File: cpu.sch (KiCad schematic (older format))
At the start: 11 parts, among them J1 Conn_02x05_Odd_Even, SW2 SW_Push, SW3 SW_Push, U1 E73-2G4M04S-52832

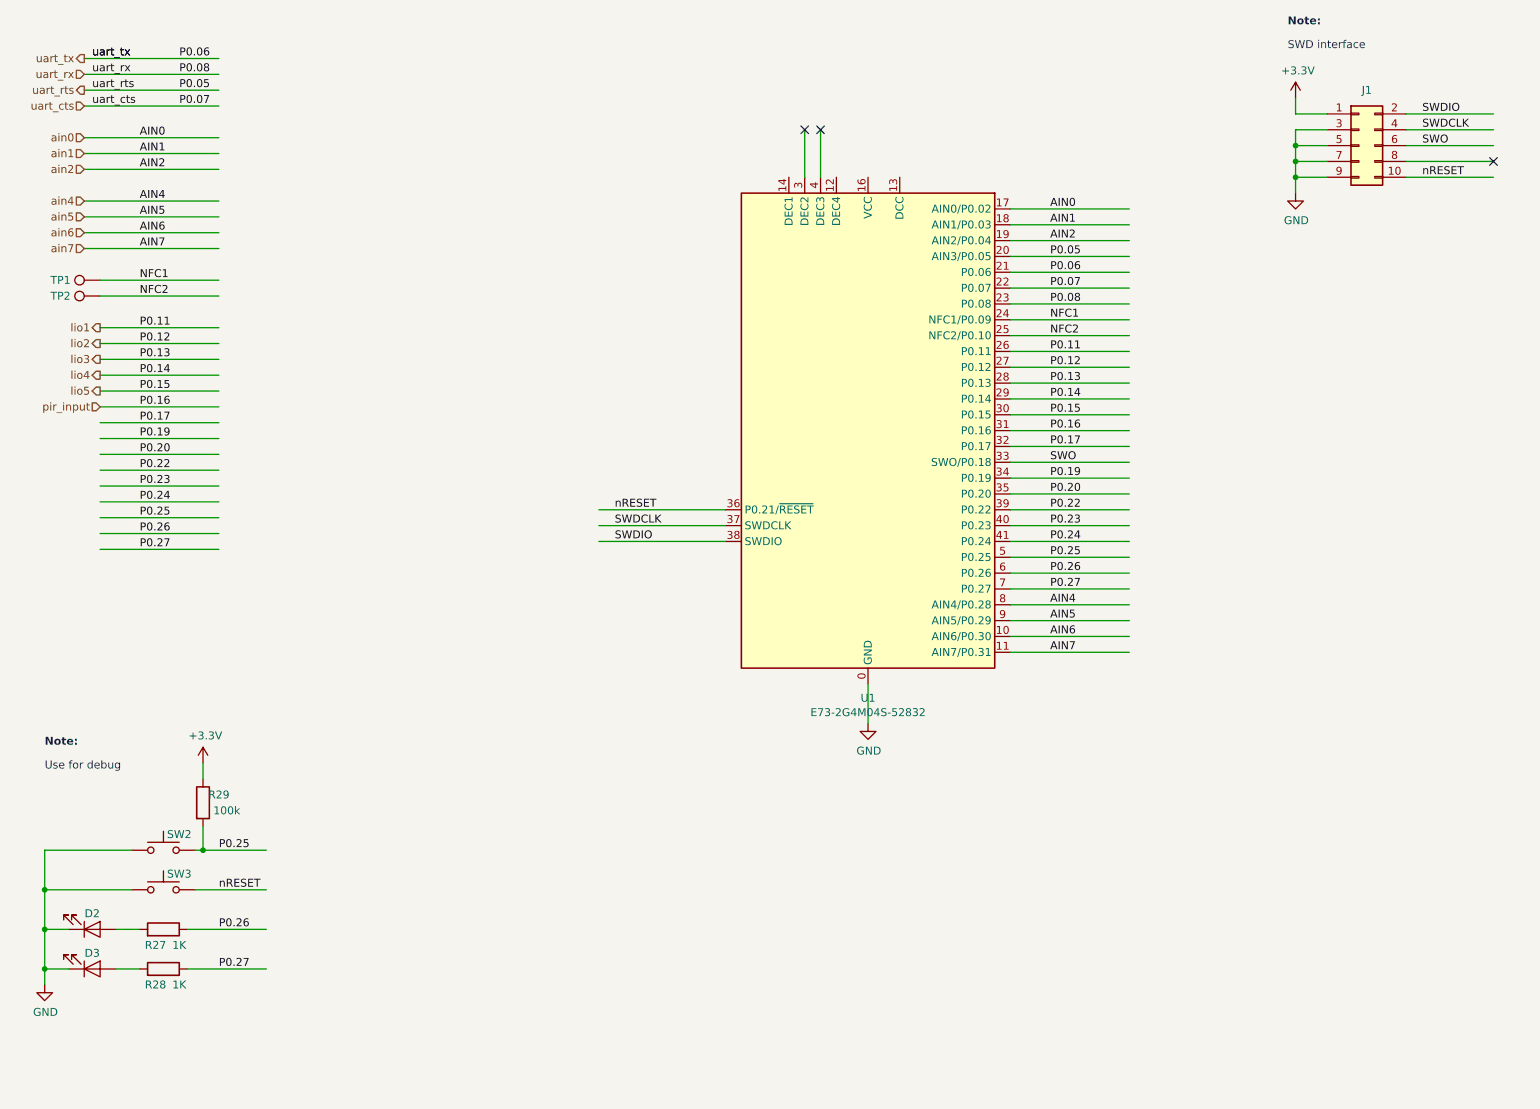
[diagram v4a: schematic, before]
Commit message: more layout + resized pcb to 100 x 80
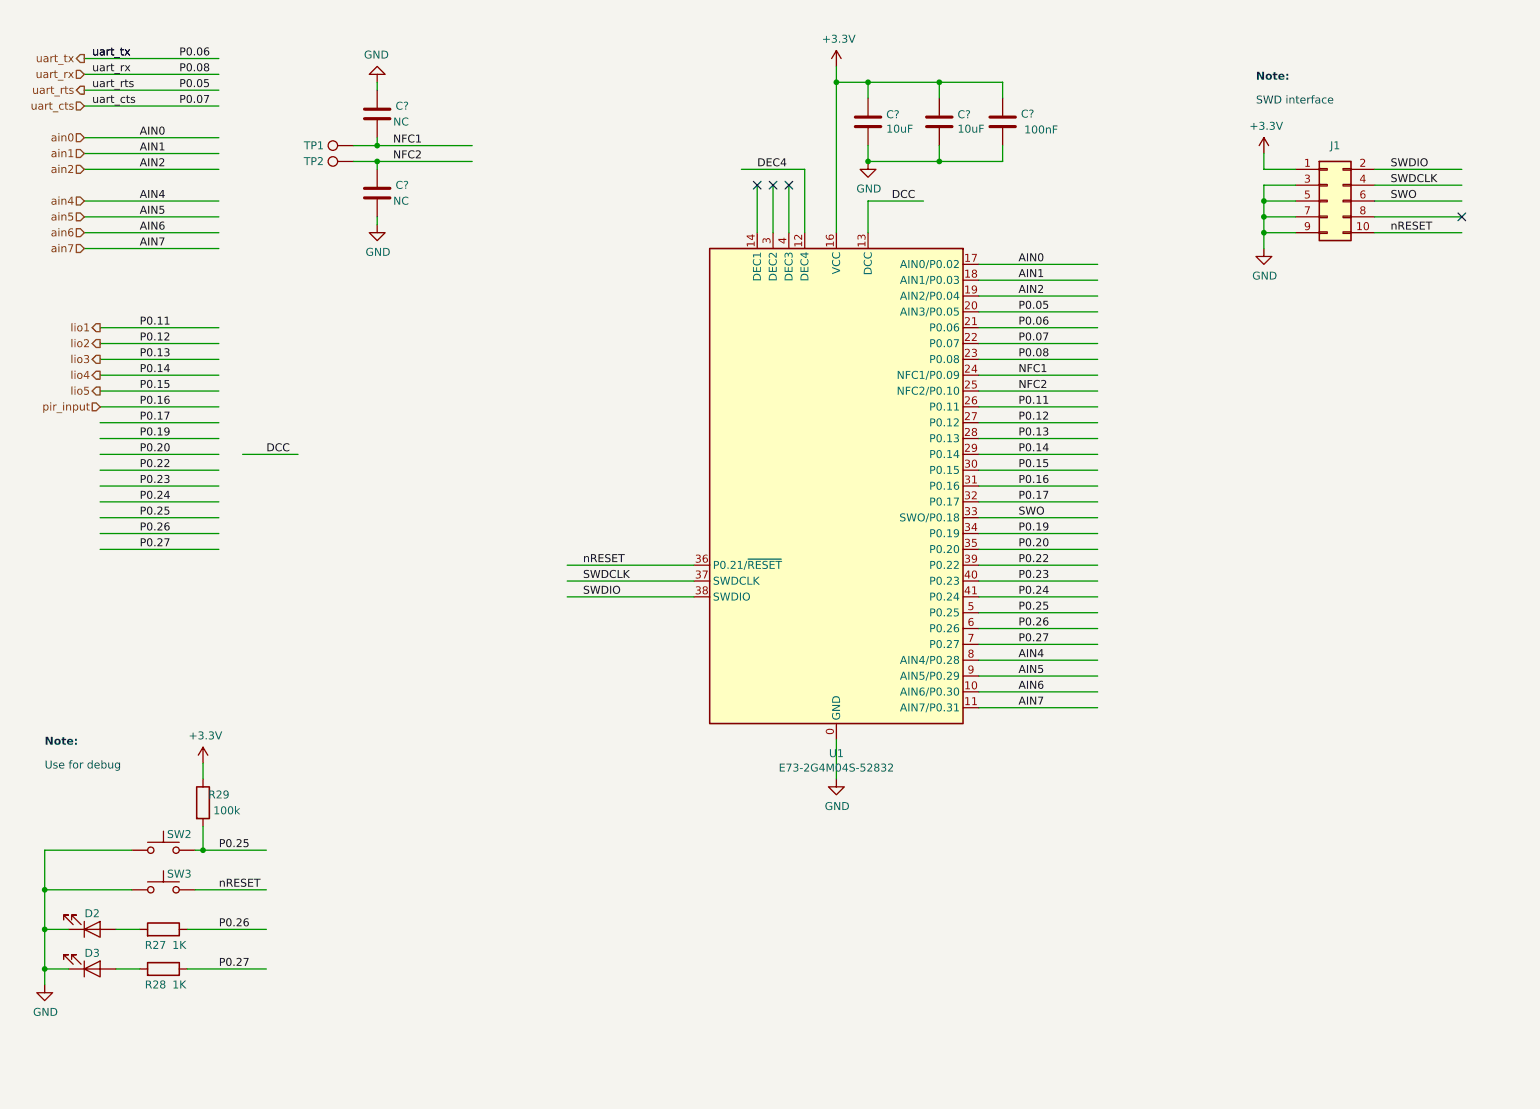
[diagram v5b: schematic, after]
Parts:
- added C? (x2): 10uF, Capacitor_SMD:C_1210_3225Metric_Pad1.42x2.65mm_HandSolder, symbol Device:C
- added C?: 100nF, Capacitor_SMD:C_0805_2012Metric_Pad1.15x1.40mm_HandSolder, symbol Device:C
- added C? (x2): NC, Capacitor_SMD:C_0603_1608Metric, symbol Device:C
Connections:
- net labels added: DCC, DEC4
- wire segments 95 -> 120
- no-connect marks 3 -> 4
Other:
- moved on the sheet: J1, TP1, TP2, U1

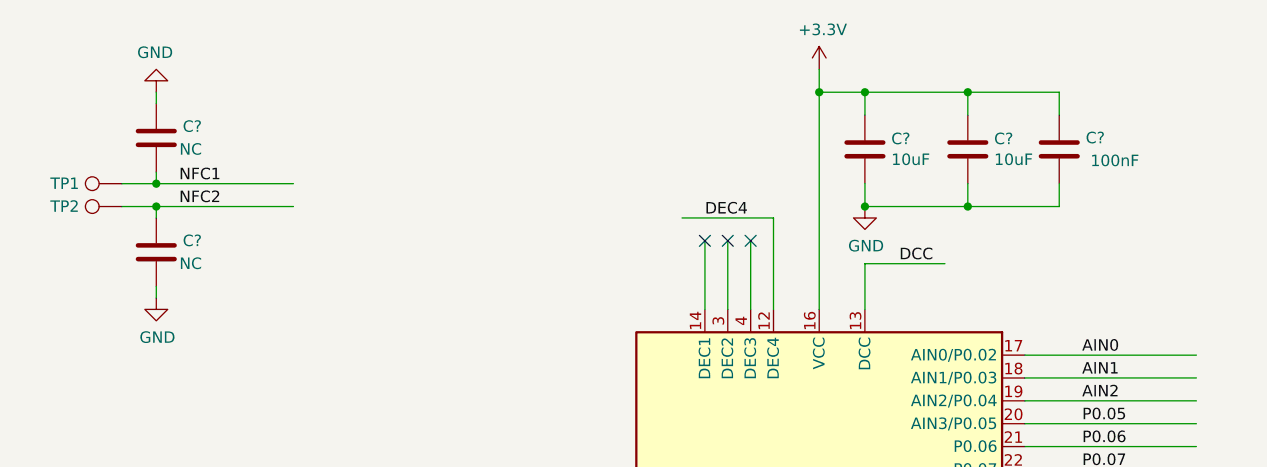
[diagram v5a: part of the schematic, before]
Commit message: changed pcb size to 100 x 70 and made progress on layout
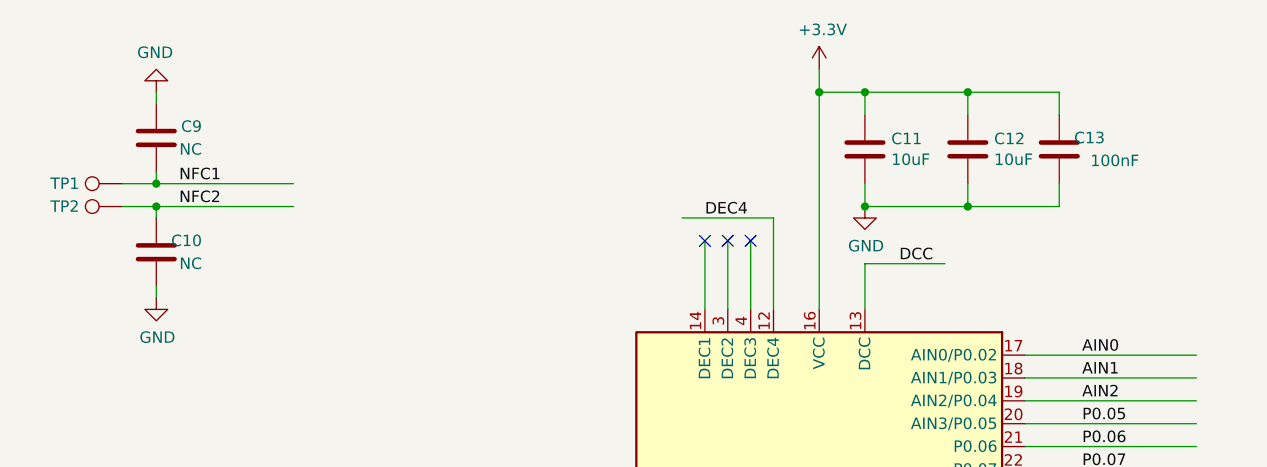
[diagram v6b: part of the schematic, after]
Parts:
- gave numbers to parts that had none: 5
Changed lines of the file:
@@
 P 6600 1500
 AR Path="/5E5BC499/5E9686F9" Ref="C?"  Part="1"
-AR Path="/5E59E010/5E9686F9" Ref="C?"  Part="1"
-F 0 "C?" H 6715 1546 50  0000 L CNN
+AR Path="/5E59E010/5E9686F9" Ref="C11"  Part="1"
+F 0 "C11" H 6715 1546 50  0000 L CNN
 F 1 "10uF" H 6715 1455 50  0000 L CNN
 F 2 "Capacitor_SMD:C_1210_3225Metric_Pad1.42x2.65mm_HandSolder" H 6638 1350 50  0001 C CNN
@@
 P 7050 1500
 AR Path="/5E5BC499/5E96C802" Ref="C?"  Part="1"
-AR Path="/5E59E010/5E96C802" Ref="C?"  Part="1"
-F 0 "C?" H 7165 1546 50  0000 L CNN
+AR Path="/5E59E010/5E96C802" Ref="C12"  Part="1"
+F 0 "C12" H 7165 1546 50  0000 L CNN
 F 1 "10uF" H 7165 1455 50  0000 L CNN
 F 2 "Capacitor_SMD:C_1210_3225Metric_Pad1.42x2.65mm_HandSolder" H 7088 1350 50  0001 C CNN
@@
 P 6400 1150
 AR Path="/5E97CE9F" Ref="#PWR?"  Part="1"
-AR Path="/5E59E010/5E97CE9F" Ref="#PWR?"  Part="1"
-F 0 "#PWR?" H 6400 1000 50  0001 C CNN
+AR Path="/5E59E010/5E97CE9F" Ref="#PWR0134"  Part="1"
+F 0 "#PWR0134" H 6400 1000 50  0001 C CNN
 F 1 "+3.3V" H 6415 1323 50  0000 C CNN
 F 2 "" H 6400 1150 50  0001 C CNN
@@
 AR Path="/5E5BC499/5E983FD2" Ref="C?"  Part="1"
 AR Path="/5E8399F7/5E983FD2" Ref="C?"  Part="1"
-AR Path="/5E59E010/5E983FD2" Ref="C?"  Part="1"
-F 0 "C?" H 7250 1450 50  0000 L CNN
+AR Path="/5E59E010/5E983FD2" Ref="C13"  Part="1"
+F 0 "C13" H 7250 1450 50  0000 L CNN
 F 1 "100nF" H 7100 1550 50  0000 L CNN
 F 2 "Capacitor_SMD:C_0805_2012Metric_Pad1.15x1.40mm_HandSolder" H 7488 1350 50  0001 C CNN
@@
 AR Path="/5E5BC499/5E9917BA" Ref="C?"  Part="1"
 AR Path="/5E8399F7/5E9917BA" Ref="C?"  Part="1"
-AR Path="/5E59E010/5E9917BA" Ref="C?"  Part="1"
-F 0 "C?" H 3300 1900 50  0000 L CNN
+AR Path="/5E59E010/5E9917BA" Ref="C10"  Part="1"
+F 0 "C10" H 3300 1900 50  0000 L CNN
 F 1 "NC" H 3300 2000 50  0000 L CNN
 F 2 "Capacitor_SMD:C_0603_1608Metric" H 3538 1800 50  0001 C CNN
@@
 AR Path="/5E5BC499/5E995EA1" Ref="C?"  Part="1"
 AR Path="/5E8399F7/5E995EA1" Ref="C?"  Part="1"
-AR Path="/5E59E010/5E995EA1" Ref="C?"  Part="1"
-F 0 "C?" H 3300 1500 50  0000 L CNN
+AR Path="/5E59E010/5E995EA1" Ref="C9"  Part="1"
+F 0 "C9" H 3300 1500 50  0000 L CNN
 F 1 "NC" H 3300 1400 50  0000 L CNN
 F 2 "Capacitor_SMD:C_0603_1608Metric" H 3538 1300 50  0001 C CNN
@@
 $EndComp
 $Comp
-L power:GND #PWR?
+L power:GND #PWR0135
 U 1 1 5E99A62D
 P 3500 2150
-F 0 "#PWR?" H 3500 1900 50  0001 C CNN
+F 0 "#PWR0135" H 3500 1900 50  0001 C CNN
 F 1 "GND" H 3505 1977 50  0000 C CNN
 F 2 "" H 3500 2150 50  0001 C CNN
@@
 	3500 1250 3500 1300
 $Comp
-L power:GND #PWR?
+L power:GND #PWR0136
 U 1 1 5E9AB701
 P 3500 1250
-F 0 "#PWR?" H 3500 1000 50  0001 C CNN
+F 0 "#PWR0136" H 3500 1000 50  0001 C CNN
 F 1 "GND" H 3505 1077 50  0000 C CNN
 F 2 "" H 3500 1250 50  0001 C CNN
@@
 P 6600 1750
 AR Path="/5E9F4A41" Ref="#PWR?"  Part="1"
-AR Path="/5E59E010/5E9F4A41" Ref="#PWR?"  Part="1"
-F 0 "#PWR?" H 6600 1500 50  0001 C CNN
+AR Path="/5E59E010/5E9F4A41" Ref="#PWR0137"  Part="1"
+F 0 "#PWR0137" H 6600 1500 50  0001 C CNN
 F 1 "GND" H 6605 1577 50  0000 C CNN
 F 2 "" H 6600 1750 50  0001 C CNN
